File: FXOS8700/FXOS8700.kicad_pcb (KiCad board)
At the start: 2 copper layers, 25.4 x 17.8 mm, 30 parts, among them J1 Conn_01x06, J2 Conn_01x04, J3 Conn_01x06, J4 Conn_01x04, Q1 BSS138DW, Q2 BSS138DW, U1 AP2127K-3.3, U2 FXOS8700

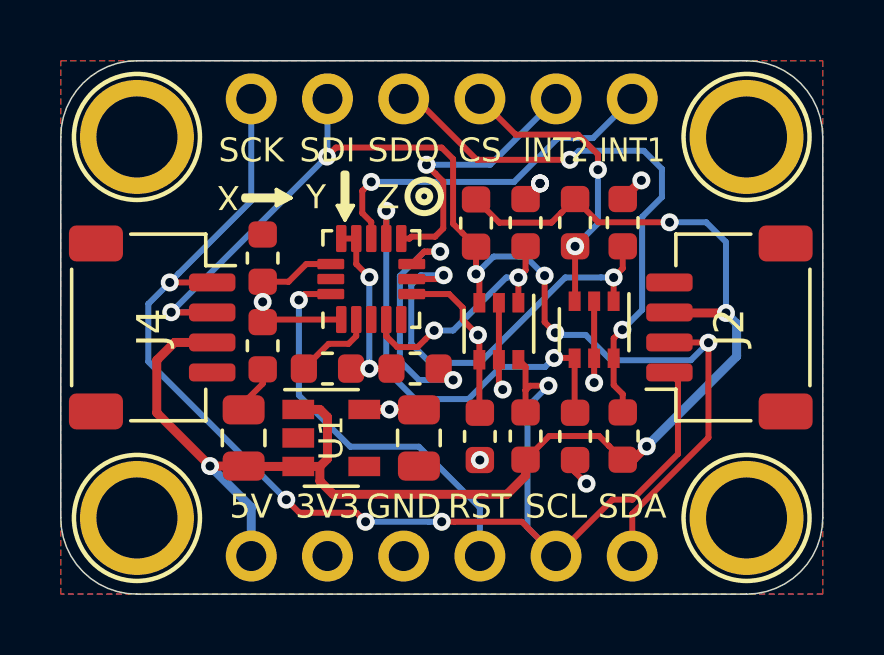
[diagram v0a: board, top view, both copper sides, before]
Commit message: Copper Pour Edits
Copper pour reduced to have 0.2mm edge clearance
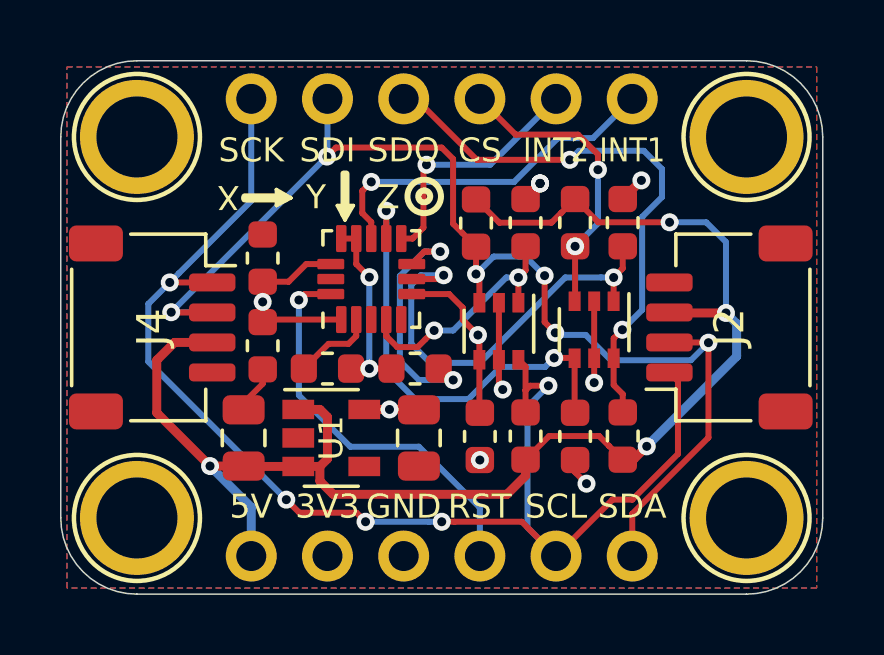
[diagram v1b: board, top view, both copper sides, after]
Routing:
- net INT2: track 9.12 -> 8.26 mm
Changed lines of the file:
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@@
     (thickness 1.6)
     (drawings 49)
-    (tracks 286)
+    (tracks 283)
     (zones 0)
     (modules 30)
@@
   (segment (start 69.088 28.3464) (end 66.8909 30.5435) (width 0.2) (layer B.Cu) (net 17))
   (segment (start 66.8909 30.5435) (end 64.77 30.5435) (width 0.2) (layer B.Cu) (net 17))
-  (segment (start 64.2035 33.0035) (end 64.267345 32.939655) (width 0.2) (layer F.Cu) (net 17))
-  (segment (start 65.329341 32.665615) (end 65.329341 31.102841) (width 0.2) (layer F.Cu) (net 17))
-  (segment (start 65.069999 30.843499) (end 64.77 30.5435) (width 0.2) (layer F.Cu) (net 17))
-  (segment (start 65.329341 31.102841) (end 65.069999 30.843499) (width 0.2) (layer F.Cu) (net 17))
-  (segment (start 65.055301 32.939655) (end 65.329341 32.665615) (width 0.2) (layer F.Cu) (net 17))
-  (segment (start 64.267345 32.939655) (end 65.055301 32.939655) (width 0.2) (layer F.Cu) (net 17))
-  (segment (start 63.9285 33.0035) (end 64.2035 33.0035) (width 0.2) (layer F.Cu) (net 17))
+  (segment (start 64.6684 30.6451) (end 64.77 30.5435) (width 0.2) (layer F.Cu) (net 17))
+  (segment (start 64.6684 32.639) (end 64.6684 30.6451) (width 0.2) (layer F.Cu) (net 17))
+  (segment (start 63.9285 33.0035) (end 64.3039 33.0035) (width 0.2) (layer F.Cu) (net 17))
+  (segment (start 64.3039 33.0035) (end 64.6684 32.639) (width 0.2) (layer F.Cu) (net 17))
   (zone (net 3) (net_name 3V3) (layer B.Cu) (hatch none 0.508)
     (connect_pads (clearance 0.15))
@@
     (polygon
       (pts
-        (xy 52.578 27.0764) (xy 77.978 27.0764) (xy 77.978 44.8564) (xy 52.578 44.8564)
+        (xy 52.7812 27.2796) (xy 77.7748 27.2796) (xy 77.7748 44.6532) (xy 52.7812 44.6532)
       )
     )
@@
     (polygon
       (pts
-        (xy 52.578 27.0764) (xy 77.978 27.0764) (xy 77.978 44.8564) (xy 52.578 44.8564)
+        (xy 52.7812 27.2796) (xy 77.7748 27.2796) (xy 77.7748 44.6532) (xy 52.7812 44.6532)
       )
     )

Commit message: Soldermask width adjusted
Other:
- rule solder_mask_min_width: 0.1 -> 0.05
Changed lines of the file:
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@@
     (pad_drill 1)
     (pad_to_mask_clearance 0)
-    (solder_mask_min_width 0.1)
+    (solder_mask_min_width 0.05)
     (aux_axis_origin 0 0)
     (visible_elements 7FFFFFFF)
